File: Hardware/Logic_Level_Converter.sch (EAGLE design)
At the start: 17 parts, among them Q1 BSS138, Q2 BSS138

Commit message: Resistor Value Changes and  Revision Code Update
Changed the vales of r5 and r9 resistors from 10k to 20k.  Added the
revision # to the schematic.
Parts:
- R5, R9: value 10K -> 20K
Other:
- note added: "V13"
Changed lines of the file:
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@@
 <part name="P+4" library="SparkFun" deviceset="VCC" device="" value="HV"/>
 <part name="R1" library="SparkFun" deviceset="RESISTOR" device="0603-RES" value="10K"/>
-<part name="R5" library="SparkFun" deviceset="RESISTOR" device="0603-RES" value="10K"/>
+<part name="R5" library="SparkFun" deviceset="RESISTOR" device="0603-RES" value="20K"/>
 <part name="R8" library="SparkFun" deviceset="RESISTOR" device="0603-RES" value="10K"/>
-<part name="R9" library="SparkFun" deviceset="RESISTOR" device="0603-RES" value="10K"/>
+<part name="R9" library="SparkFun" deviceset="RESISTOR" device="0603-RES" value="20K"/>
 <part name="GND1" library="SparkFun" deviceset="GND" device=""/>
 <part name="GND2" library="SparkFun" deviceset="GND" device=""/>
@@
 <text x="251.46" y="172.72" size="1.778" layer="97">BOM changes, NO</text>
 <text x="251.46" y="167.64" size="1.778" layer="97">New Stencil, NO</text>
+<text x="238.76" y="7.62" size="2.54" layer="94" font="vector">V13</text>
 </plain>
 <instances>

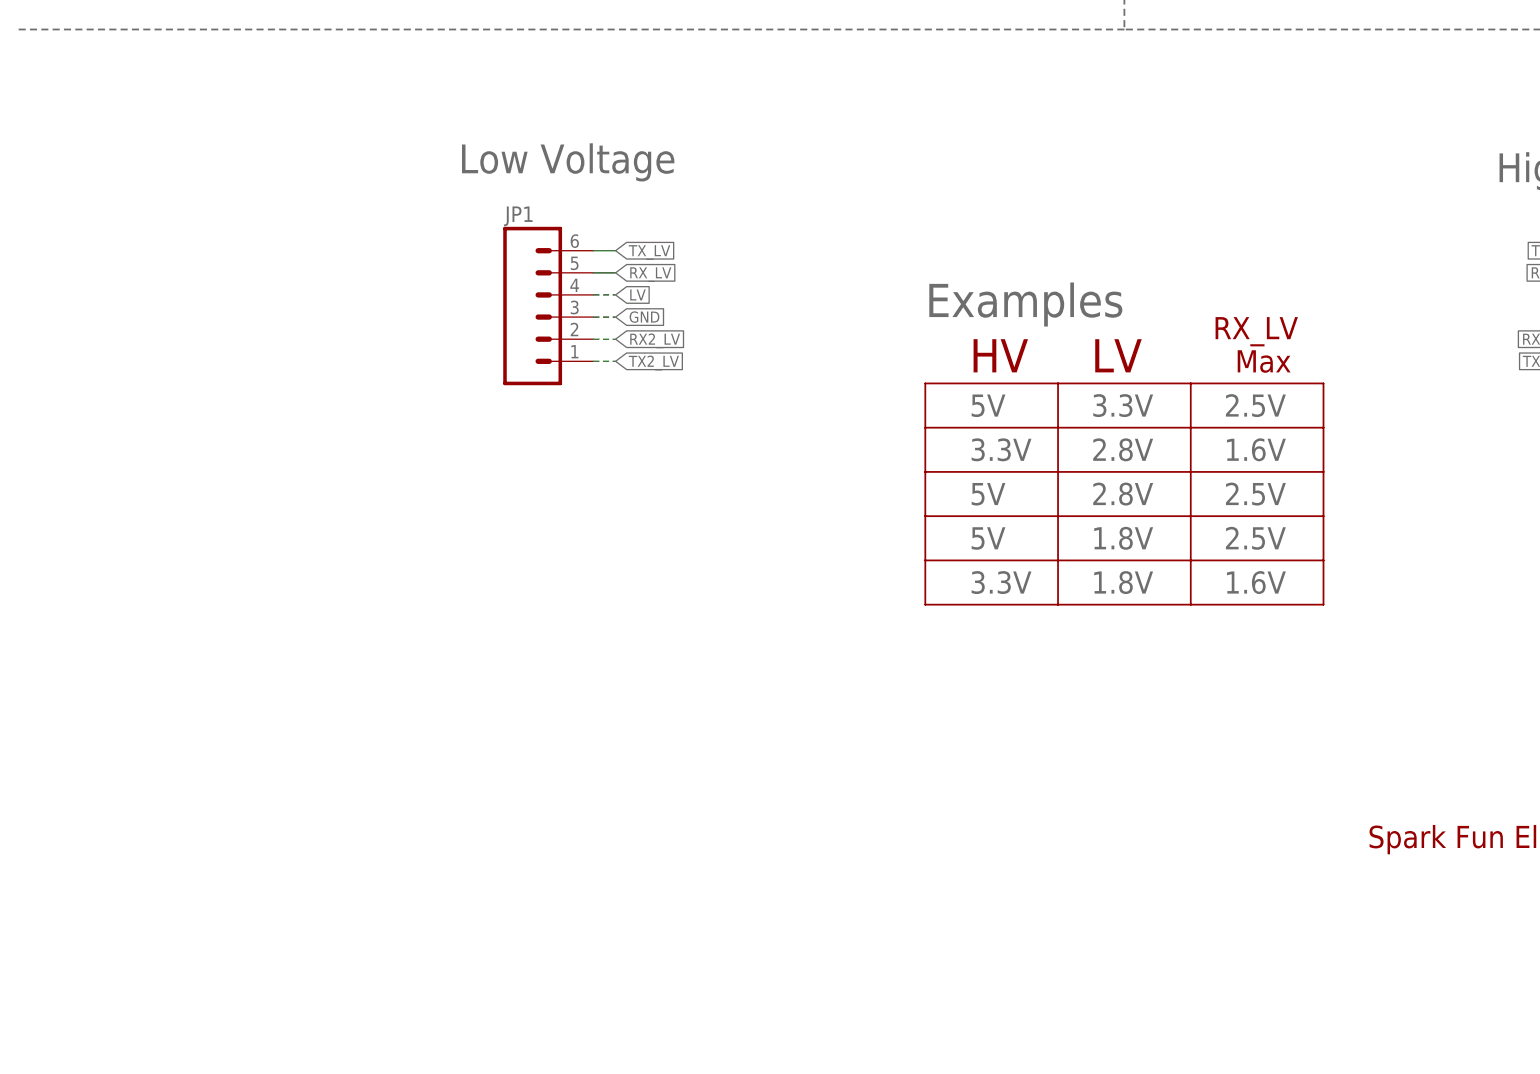
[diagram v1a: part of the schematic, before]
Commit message: Updated Voltage Table / Added Creative Commons/Rev
Changed the Example Voltage table to reflect the new resistor values as
well as added an equation for reference.  Added the creative commons
license and designed by/revised by names.
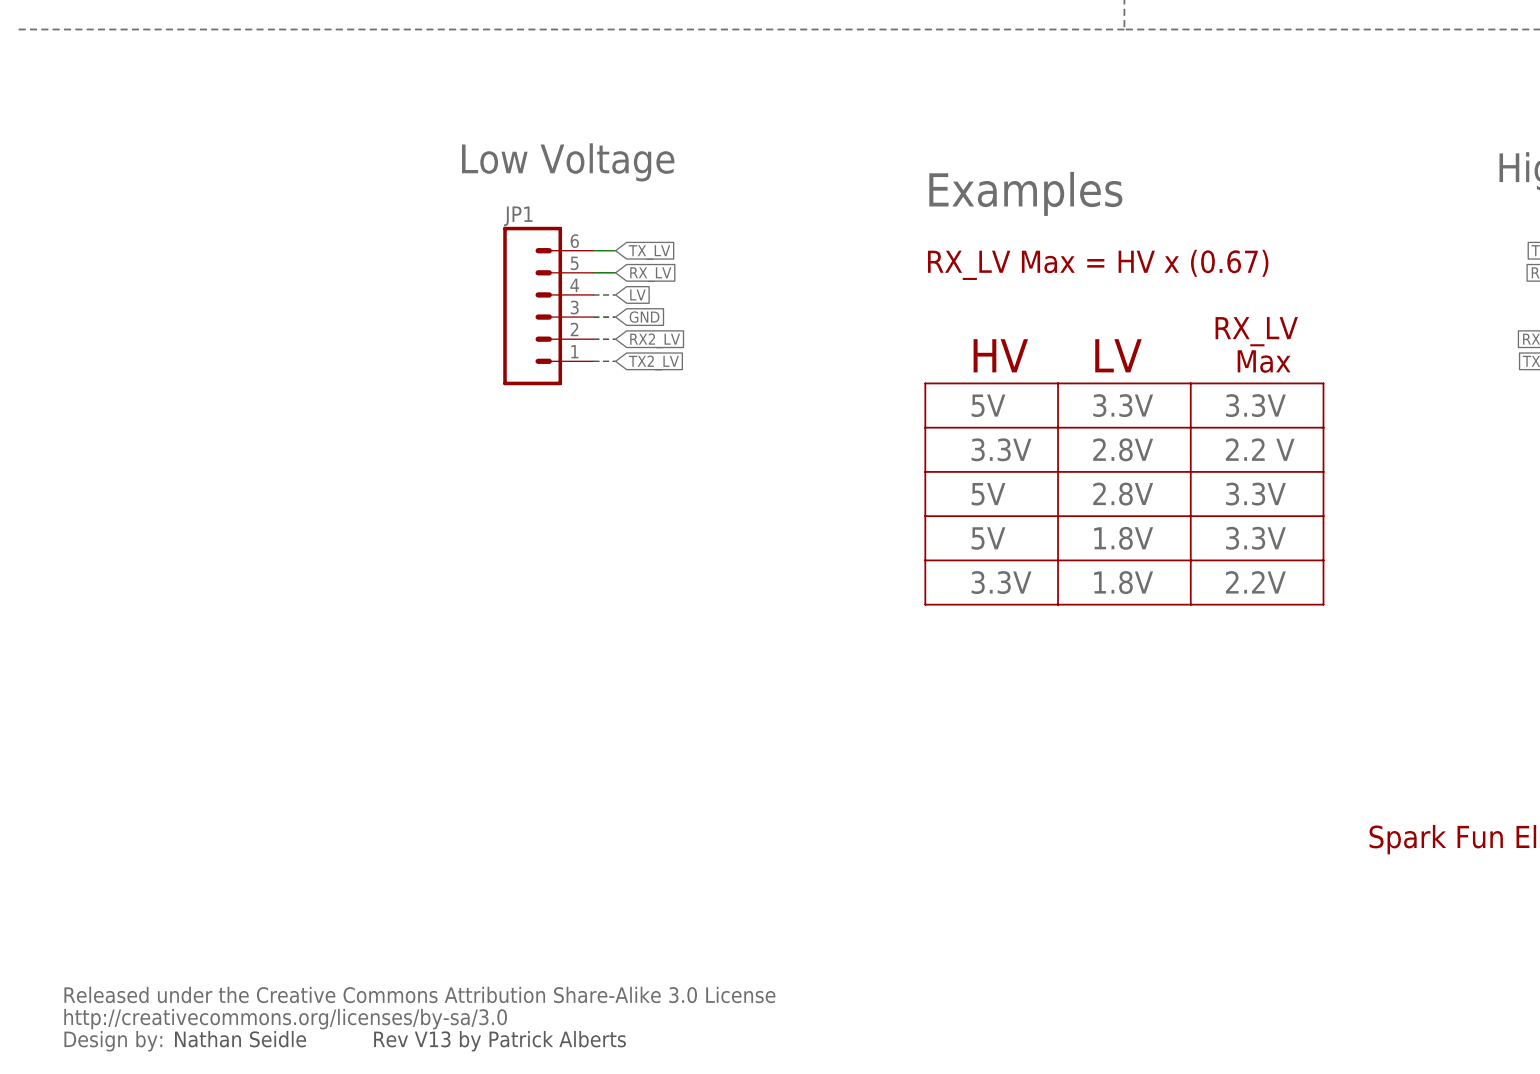
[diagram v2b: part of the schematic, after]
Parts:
- added CC_TEXT1: CREATIVE_COMMONS, SparkFun-Aesthetics:CREATIVE_COMMONS
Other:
- note added: "2.2 V"
- note added: "2.2V"
- note added: "Nathan Seidle"
- note added: "RX_LV Max = HV x (0.67)"
- note added: "Rev V13 by Patrick Alberts"
- note removed: "1.6V"
- note removed: "2.5V"
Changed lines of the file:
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@@
 <layer number="144" name="Drill_legend" color="7" fill="1" visible="yes" active="yes"/>
 <layer number="151" name="HeatSink" color="7" fill="1" visible="yes" active="yes"/>
+<layer number="199" name="Contour" color="7" fill="1" visible="no" active="yes"/>
 <layer number="200" name="200bmp" color="1" fill="10" visible="no" active="no"/>
 <layer number="201" name="201bmp" color="2" fill="1" visible="no" active="no"/>
@@
 <part name="U$2" library="SparkFun-Aesthetics" deviceset="OSHW-LOGO" device="S"/>
 <part name="JP5" library="SparkFun-Aesthetics" deviceset="LOGO-SFE" device="NW2" value="LOGO-SFENW2"/>
+<part name="CC_TEXT1" library="SparkFun-Aesthetics" deviceset="CREATIVE_COMMONS" device=""/>
 </parts>
 <sheets>
@@
 <text x="169.672" y="104.394" size="3.302" layer="95">High Voltage</text>
 <text x="50.546" y="105.41" size="3.302" layer="95">Low Voltage</text>
-<text x="104.14" y="88.9" size="3.81" layer="95">Examples</text>
+<text x="104.14" y="101.6" size="3.81" layer="95">Examples</text>
 <text x="109.22" y="82.55" size="3.81" layer="94">HV</text>
 <text x="123.19" y="82.55" size="3.81" layer="94">LV</text>
@@
 <text x="109.22" y="77.47" size="2.54" layer="95">5V</text>
 <text x="123.19" y="77.47" size="2.54" layer="95">3.3V</text>
-<text x="138.43" y="77.47" size="2.54" layer="95">2.5V</text>
+<text x="138.43" y="77.47" size="2.54" layer="95">3.3V</text>
 <text x="109.22" y="72.39" size="2.54" layer="95">3.3V</text>
 <text x="109.22" y="67.31" size="2.54" layer="95">5V</text>
 <text x="123.19" y="72.39" size="2.54" layer="95">2.8V</text>
 <text x="123.19" y="67.31" size="2.54" layer="95">2.8V</text>
-<text x="138.43" y="72.39" size="2.54" layer="95">1.6V</text>
-<text x="138.43" y="67.31" size="2.54" layer="95">2.5V</text>
+<text x="138.43" y="72.39" size="2.54" layer="95">2.2 V</text>
+<text x="138.43" y="67.31" size="2.54" layer="95">3.3V</text>
 <text x="109.22" y="62.23" size="2.54" layer="95">5V</text>
 <text x="123.19" y="62.23" size="2.54" layer="95">1.8V</text>
-<text x="138.43" y="62.23" size="2.54" layer="95">2.5V</text>
+<text x="138.43" y="62.23" size="2.54" layer="95">3.3V</text>
 <text x="109.22" y="57.15" size="2.54" layer="95">3.3V</text>
 <text x="123.19" y="57.15" size="2.54" layer="95">1.8V</text>
-<text x="138.43" y="57.15" size="2.54" layer="95">1.6V</text>
+<text x="138.43" y="57.15" size="2.54" layer="95">2.2V</text>
 <text x="251.46" y="180.34" size="1.778" layer="97">Changes made to v12</text>
 <text x="251.46" y="177.8" size="1.778" layer="97">Library update, increased annular rings</text>
@@
 <text x="251.46" y="167.64" size="1.778" layer="97">New Stencil, NO</text>
 <text x="238.76" y="7.62" size="2.54" layer="94" font="vector">V13</text>
+<text x="104.14" y="93.98" size="2.54" layer="94" font="vector">RX_LV Max = HV x (0.67)</text>
+<text x="17.78" y="5.08" size="1.778" layer="97" font="vector">Nathan Seidle </text>
+<text x="40.64" y="5.08" size="1.778" layer="97" font="vector">Rev V13 by Patrick Alberts</text>
 </plain>
 <instances>
@@
 <instance part="U$2" gate="G$1" x="236.22" y="45.72"/>
 <instance part="JP5" gate="G$1" x="210.82" y="40.64"/>
+<instance part="CC_TEXT1" gate="G$1" x="5.08" y="5.08"/>
 </instances>
 <busses>

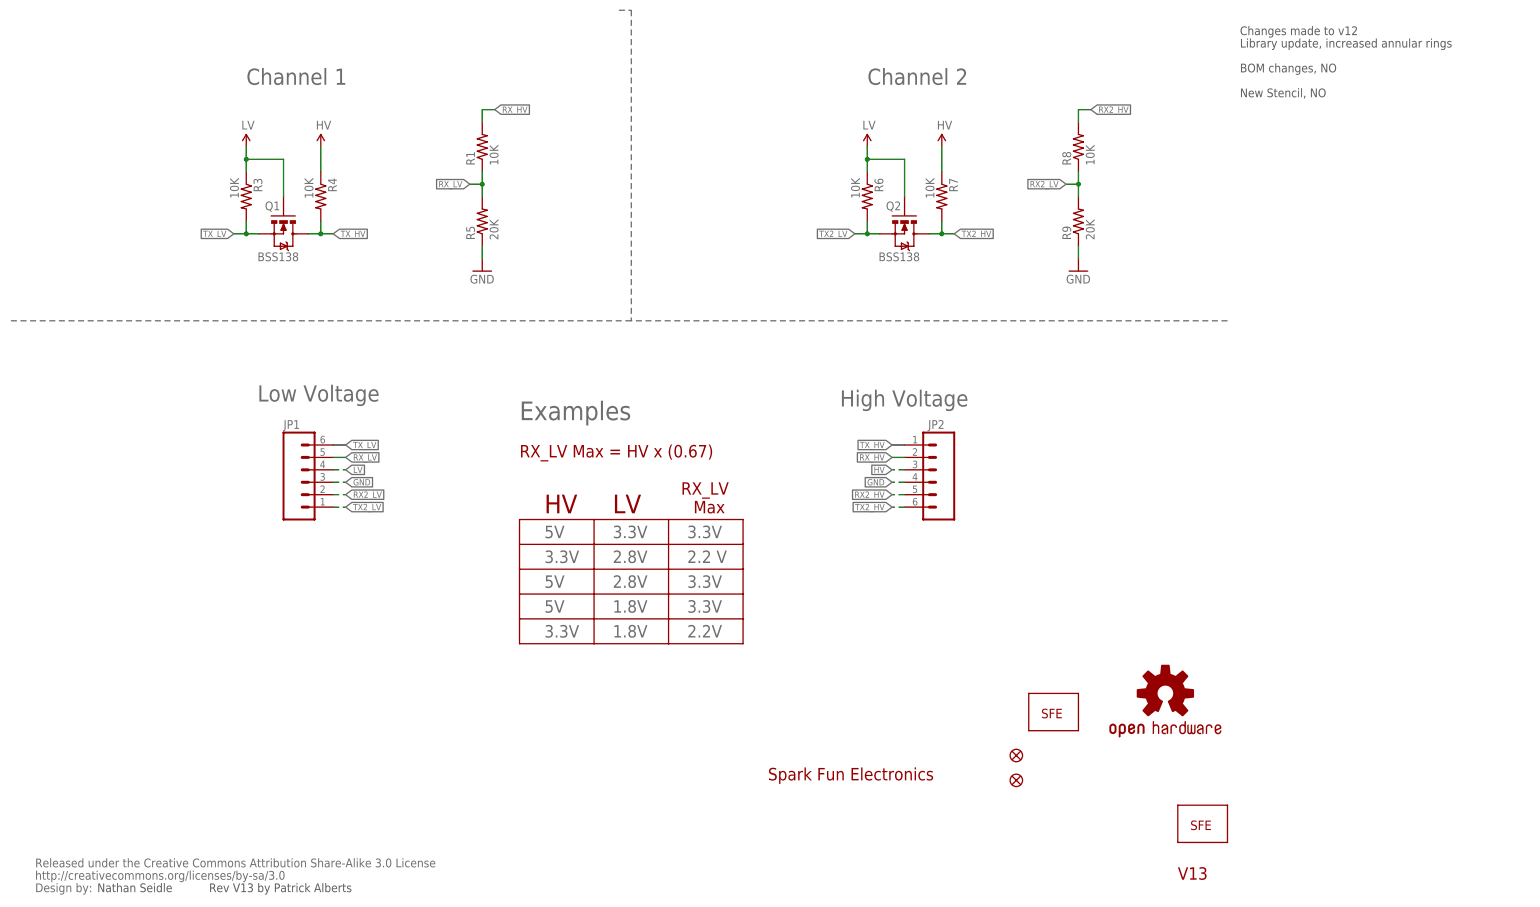
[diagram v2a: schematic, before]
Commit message: Small typo updates to schematic.
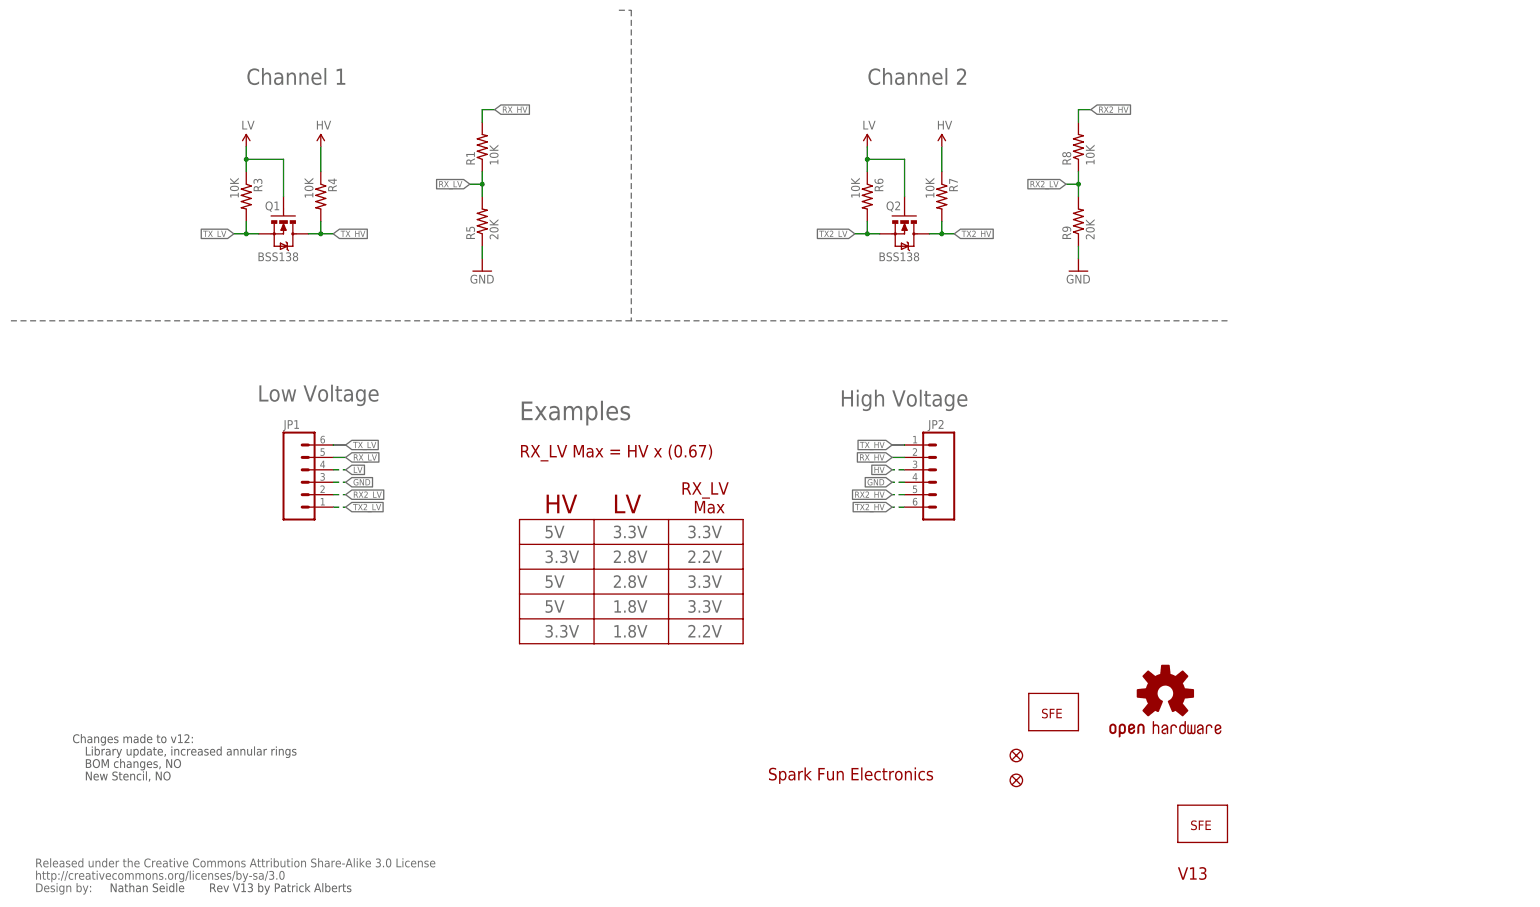
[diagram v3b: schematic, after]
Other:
- note added: "Changes made to v12:"
- note removed: "2.2 V"
- note removed: "Changes made to v12"
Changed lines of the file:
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@@
 <?xml version="1.0" encoding="utf-8"?>
 <!DOCTYPE eagle SYSTEM "eagle.dtd">
-<eagle version="6.4">
+<eagle version="6.5.0">
 <drawing>
 <settings>
@@
 <text x="123.19" y="72.39" size="2.54" layer="95">2.8V</text>
 <text x="123.19" y="67.31" size="2.54" layer="95">2.8V</text>
-<text x="138.43" y="72.39" size="2.54" layer="95">2.2 V</text>
+<text x="138.43" y="72.39" size="2.54" layer="95">2.2V</text>
 <text x="138.43" y="67.31" size="2.54" layer="95">3.3V</text>
 <text x="109.22" y="62.23" size="2.54" layer="95">5V</text>
@@
 <text x="123.19" y="57.15" size="2.54" layer="95">1.8V</text>
 <text x="138.43" y="57.15" size="2.54" layer="95">2.2V</text>
-<text x="251.46" y="180.34" size="1.778" layer="97">Changes made to v12</text>
-<text x="251.46" y="177.8" size="1.778" layer="97">Library update, increased annular rings</text>
-<text x="251.46" y="172.72" size="1.778" layer="97">BOM changes, NO</text>
-<text x="251.46" y="167.64" size="1.778" layer="97">New Stencil, NO</text>
+<text x="12.7" y="35.56" size="1.778" layer="97">Changes made to v12:</text>
+<text x="15.24" y="33.02" size="1.778" layer="97">Library update, increased annular rings</text>
+<text x="15.24" y="30.48" size="1.778" layer="97">BOM changes, NO</text>
+<text x="15.24" y="27.94" size="1.778" layer="97">New Stencil, NO</text>
 <text x="238.76" y="7.62" size="2.54" layer="94" font="vector">V13</text>
 <text x="104.14" y="93.98" size="2.54" layer="94" font="vector">RX_LV Max = HV x (0.67)</text>
-<text x="17.78" y="5.08" size="1.778" layer="97" font="vector">Nathan Seidle </text>
+<text x="20.32" y="5.08" size="1.778" layer="97" font="vector">Nathan Seidle </text>
 <text x="40.64" y="5.08" size="1.778" layer="97" font="vector">Rev V13 by Patrick Alberts</text>
 </plain>
